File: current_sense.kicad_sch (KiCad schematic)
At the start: 1 part, among them IC4 AD8030ARZ

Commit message: Initial layout
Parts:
- added C25, C6, C7: TBD, Capacitor_SMD:C_0603_1608Metric, symbol Device:C_Small
- added C26, C27, C28, C5: 0.1u, Capacitor_SMD:C_0603_1608Metric, symbol Device:C_Small
- added IC5: LTC6655BHMS8-1.25#TRPBF, BLDC-Motor-Driver:LTC6655, symbol BLDC-Motor-Driver_v2:LTC6655BHMS8-1.25#TRPBF
- added IC9: AD8030ARZ, BLDC-Motor-Driver:AD8030ARZ-SOIC8, symbol bldc-driver-pcb:AD8030ARZ
- added R20, R21, R22, R23, R25, R26, R27, R28, R29, R30, R31, R32, R35, R36, R37: 10k, Resistor_SMD:R_0603_1608Metric, symbol Device:R_US
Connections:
- net CSA_PH_A_VOUT: now reaches IC4.1 (VOUT1)
- net CSA_PH_A_VOUT: now also C6.2, R22.2
- net at IC4.2 (-IN_1): now also C6.1, R20.2, R22.1
- net at IC4.3 (+IN_1): now also R21.1, R23.2
- net GND: now reaches IC4.4 (-VS)
- net GND: now also C26.1, C27.1, C28.1, C5.1, IC5.3 (GND_1), IC5.4 (GND_2), IC5.5 (GND_3), IC5.8 (GND_4), IC9.4 (-VS), R30.2
- net at IC4.5 (+IN_2): now also R25.2, R36.2
- net at IC4.6 (-IN_2): now also C7.2, R26.1, R35.2
- net CSA_PH_B_VOUT: now reaches IC4.7 (+VOUT_2)
- net CSA_PH_B_VOUT: now also C7.1, R35.1
- net +3V3: now reaches IC4.8 (+VS)
- net +3V3: now also C26.2, C27.2, C5.2, IC5.2 (VIN), IC9.8 (+VS), R31.1, R32.1
- new net: IC9.3 (+IN_1), R28.1, R37.2
- new net: C25.1, IC9.2 (-IN_1), R27.2, R29.1
- new net: IC5.1 (~{SHDN}), R32.2
- new net: IC9.5 (+IN_2), R30.1, R31.2
- new net: IC9.6 (-IN_2), IC9.7 (+VOUT_2)
- new net CSA_PH_A_IN+: R21.2
- new net CSA_PH_A_IN-: R20.1
- new net CSA_PH_B_IN+: R25.1
- new net CSA_PH_B_IN-: R26.2
- new net CSA_PH_C_IN+: R28.2
- new net CSA_PH_C_IN-: R27.1
- new net CSA_PH_C_VOUT: C25.2, IC9.1 (VOUT1), R29.2
- new net VREF: C28.2, IC5.6 (VOUT_S), IC5.7 (VOUT_F), R23.1, R36.1, R37.1
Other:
- moved on the sheet: IC4

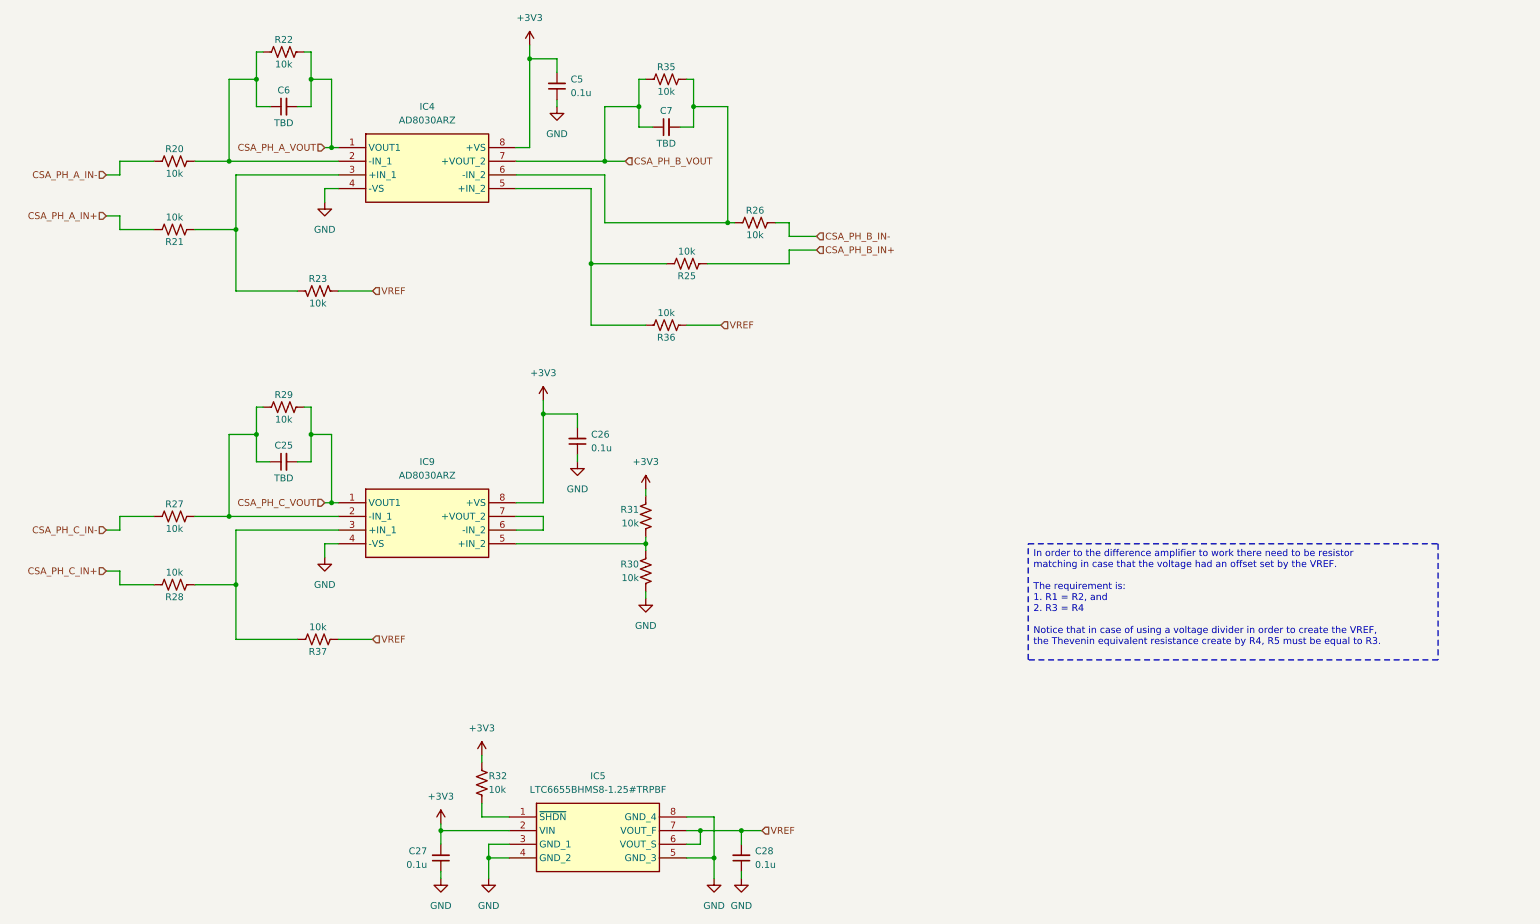
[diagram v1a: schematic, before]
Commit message: Almost all routing done
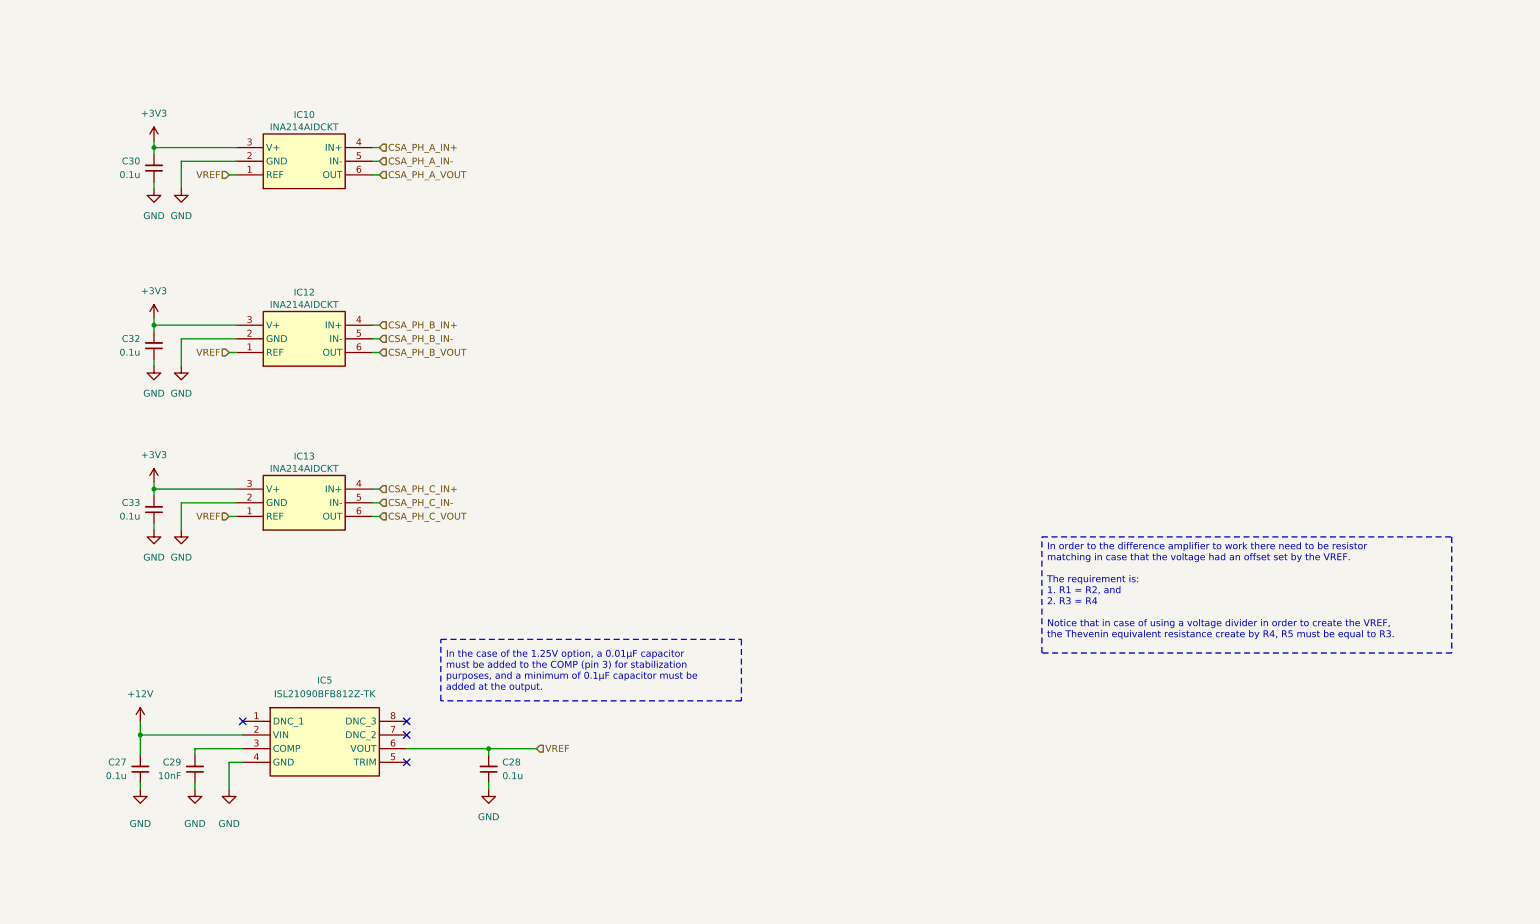
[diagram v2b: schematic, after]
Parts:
- removed C25, C6, C7: TBD, Capacitor_SMD:C_0603_1608Metric, symbol Device:C_Small
- removed C26, C5: 0.1u, Capacitor_SMD:C_0603_1608Metric, symbol Device:C_Small
- removed IC4: AD8030ARZ, BLDC-Motor-Driver:AD8030ARZ-SOIC8, symbol BLDC-Motor-Driver_v2:AD8030ARZ
- removed IC5: LTC6655BHMS8-1.25#TRPBF, BLDC-Motor-Driver:LTC6655, symbol BLDC-Motor-Driver_v2:LTC6655BHMS8-1.25#TRPBF
- removed IC9: AD8030ARZ, BLDC-Motor-Driver:AD8030ARZ-SOIC8, symbol bldc-driver-pcb:AD8030ARZ
- removed R20, R21, R22, R23, R25, R26, R27, R28, R29, R30, R31, R32, R35, R36, R37: 10k, Resistor_SMD:R_0603_1608Metric, symbol Device:R_US
- added C29: 10nF, Capacitor_SMD:C_0603_1608Metric, symbol Device:C_Small
- added C30, C32, C33: 0.1u, Capacitor_SMD:C_0603_1608Metric, symbol Device:C_Small
- added IC10, IC12, IC13: INA214AIDCKT, BLDC-Motor-Driver:INA214AIDCKT, symbol BLDC-Motor-Driver_v2:INA214AIDCKT
- added IC5: ISL21090BFB812Z-TK, BLDC-Motor-Driver:ISL21090, symbol BLDC-Motor-Driver_v2:ISL21090BFB812Z-TK
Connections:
- net +3V3: now also C30.2, C32.2, C33.2, IC10.3 (V+), IC12.3 (V+), IC13.3 (V+); no longer C27.2
- net CSA_PH_A_IN+: now also IC10.4 (IN+)
- net CSA_PH_A_IN-: now also IC10.5 (IN-)
- net CSA_PH_A_VOUT: now also IC10.6 (OUT)
- net CSA_PH_B_IN+: now also IC12.4 (IN+)
- net CSA_PH_B_IN-: now also IC12.5 (IN-)
- net CSA_PH_B_VOUT: now also IC12.6 (OUT)
- net CSA_PH_C_IN+: now also IC13.4 (IN+)
- net CSA_PH_C_IN-: now also IC13.5 (IN-)
- net CSA_PH_C_VOUT: now also IC13.6 (OUT)
- net GND: now also C29.1, C30.1, C32.1, C33.1, IC10.2 (GND), IC12.2 (GND), IC13.2 (GND), IC5.4 (GND)
- net VREF: now also IC10.1 (REF), IC12.1 (REF), IC13.1 (REF), IC5.6 (VOUT)
- new net: C29.2, IC5.3 (COMP)
- new net +12V: C27.2, IC5.2 (VIN)
- no-connect marks 0 -> 4
